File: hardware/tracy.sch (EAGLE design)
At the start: 68 parts, among them IC1 SIM900, J1 U.FL, J2 U.FL, Q4 si2305cd, T2 BC846, U1 SPX5205 3v3, U2 3339, U3 TC1014 2V8, Y1 32768Hz CFPX-217 12.5pF

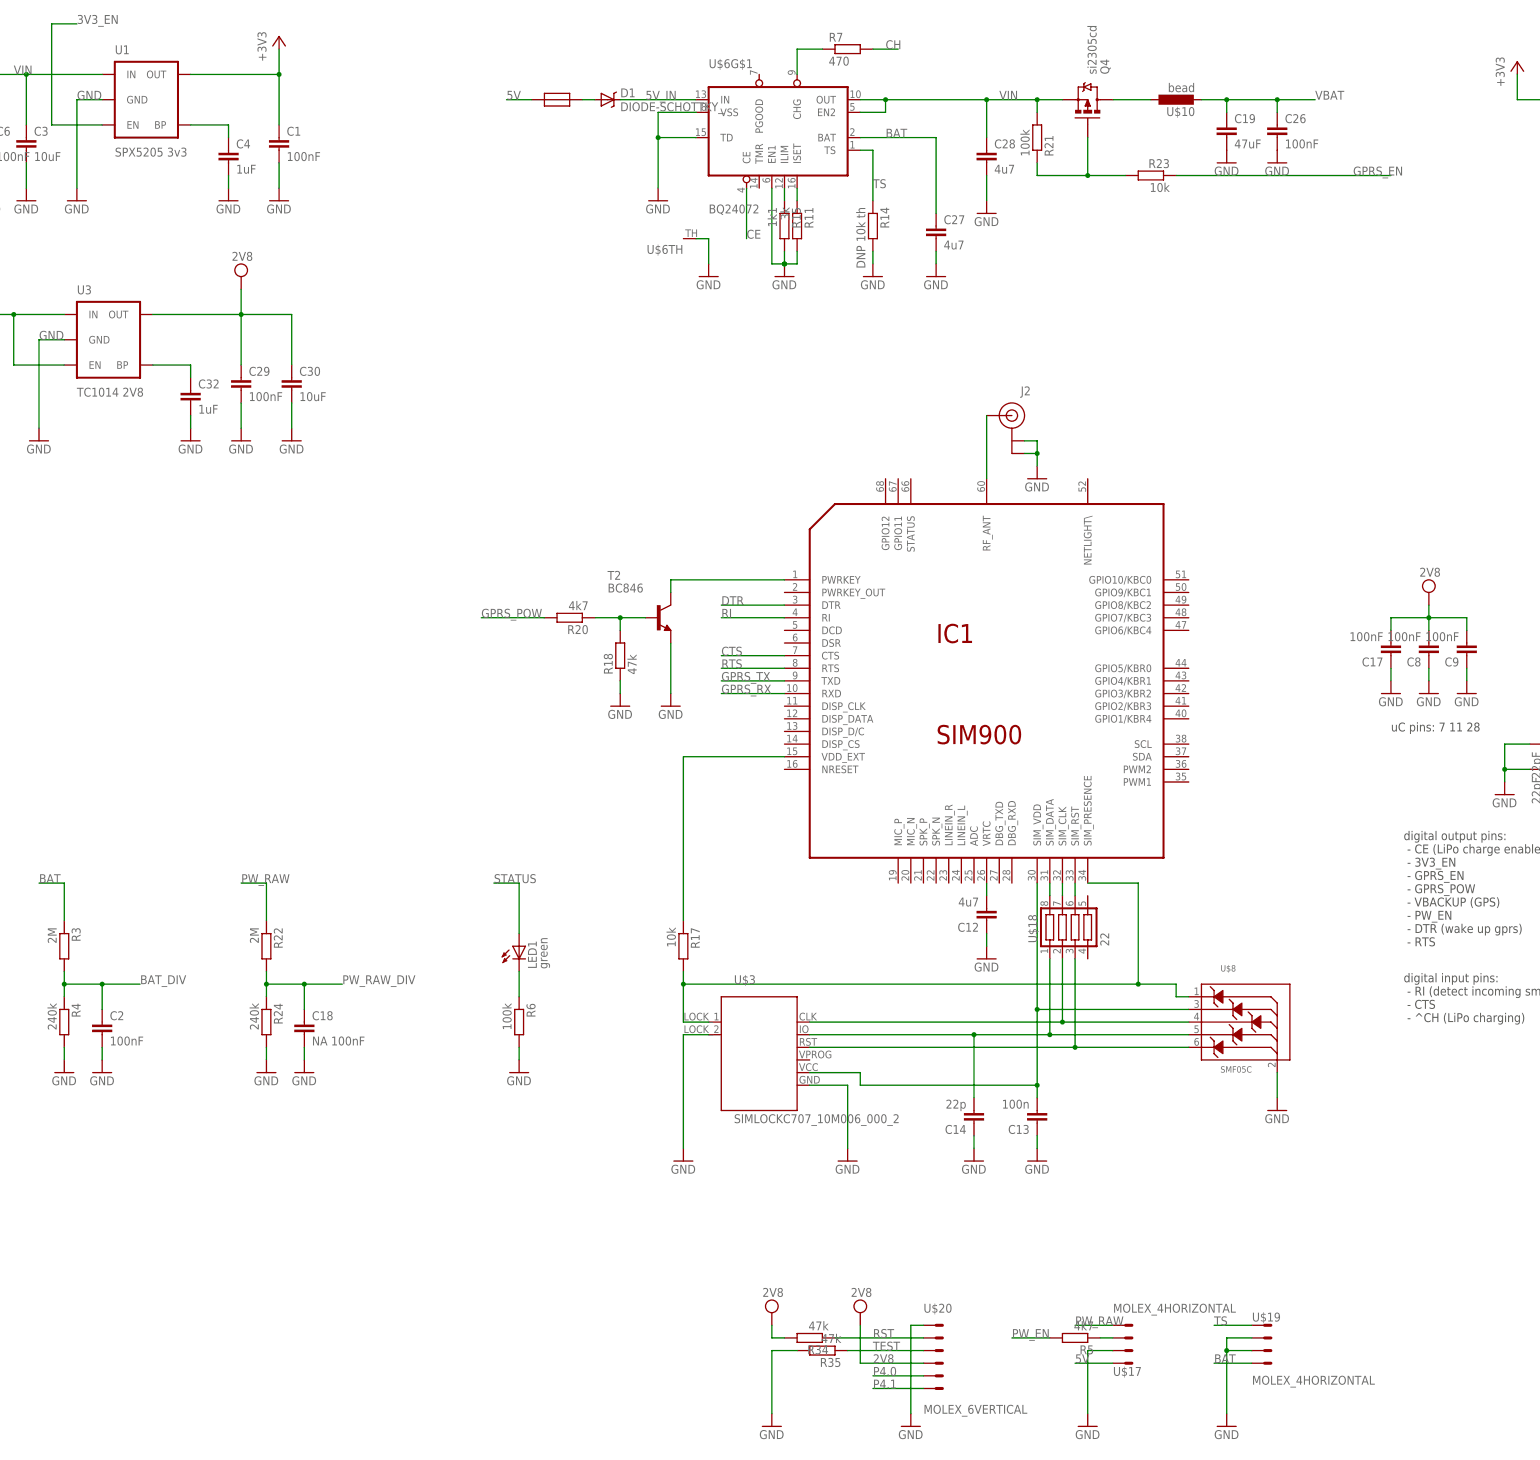
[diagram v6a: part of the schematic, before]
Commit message: add silkscreen
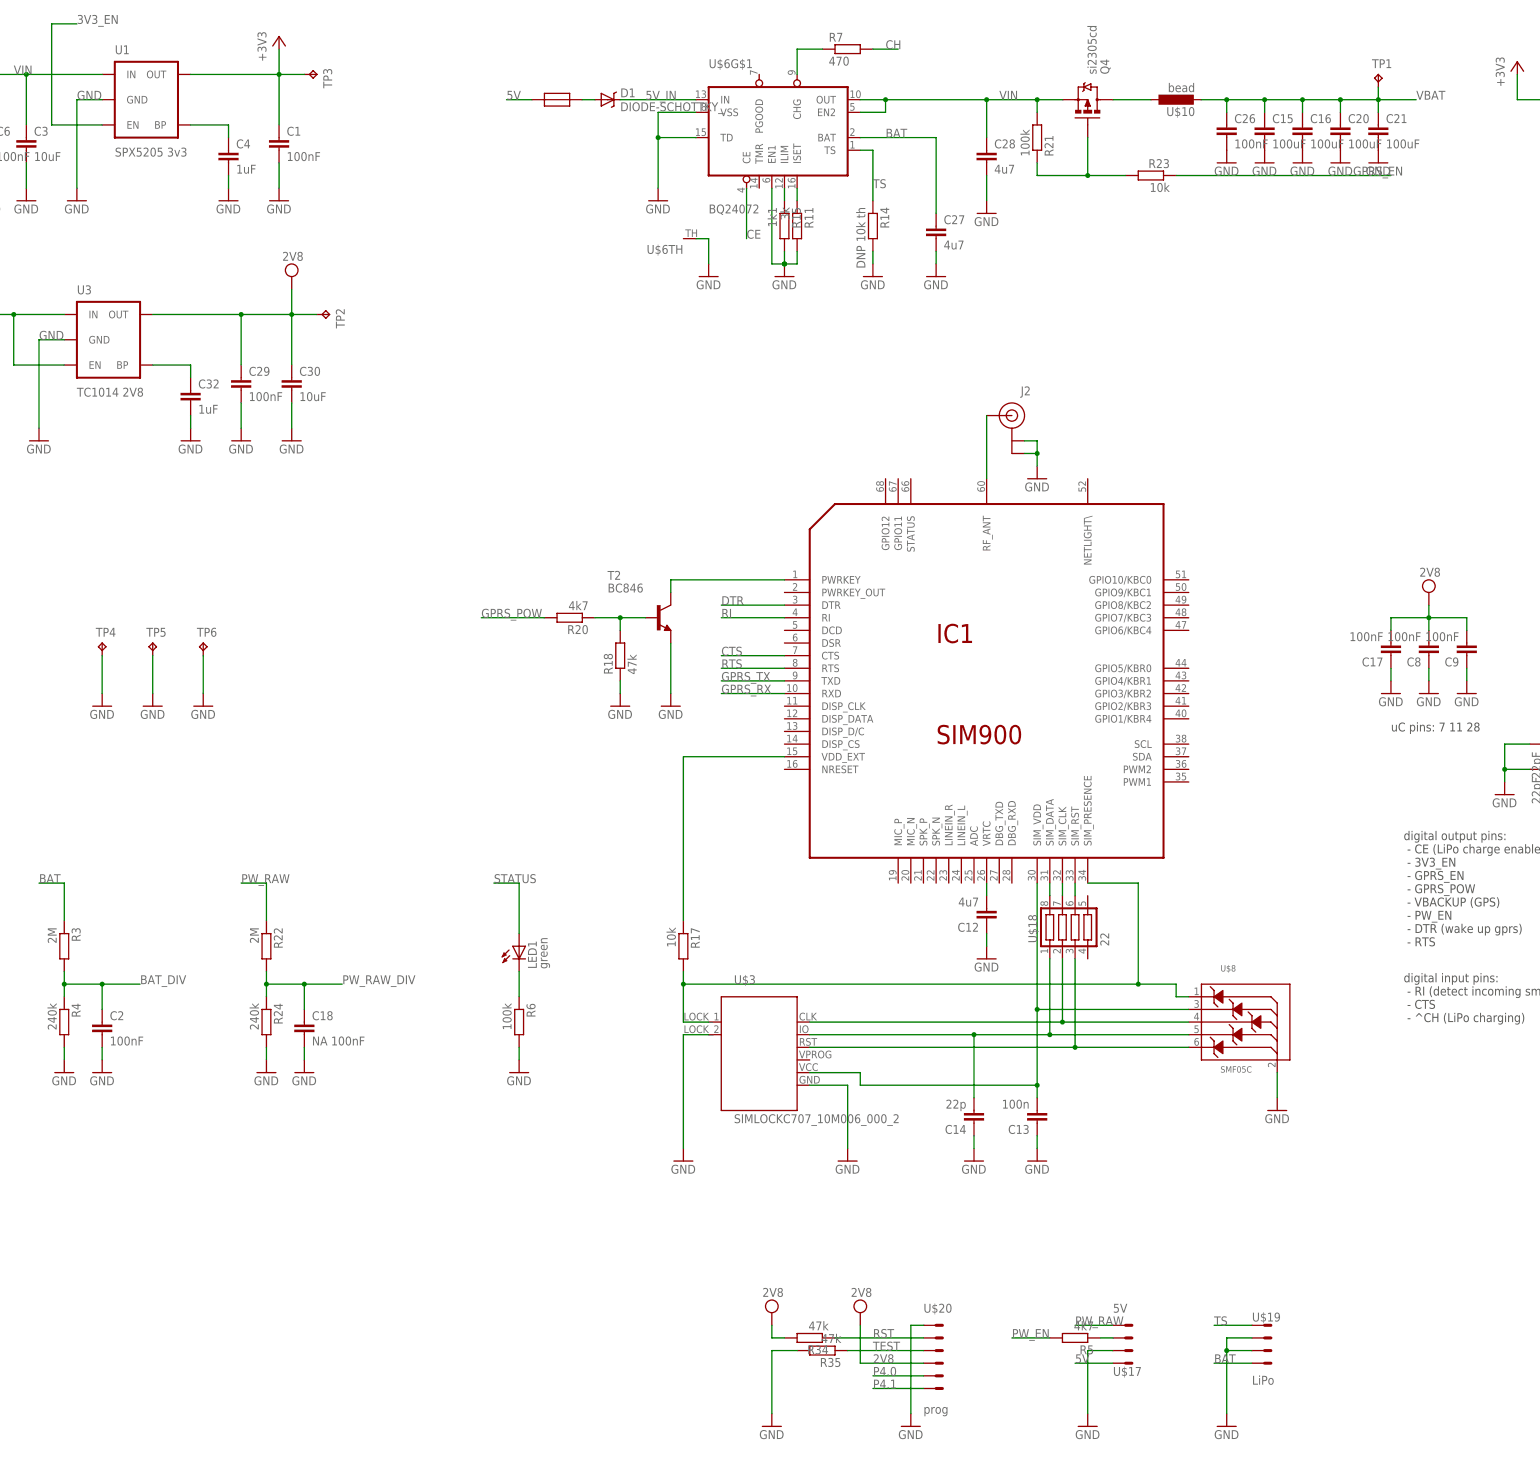
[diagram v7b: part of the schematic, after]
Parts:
- removed C19: 47uF, rcl:C-EUC1206
- added C15, C16, C20, C21: 100uF, rcl:C-EUC1206
- added TP1, TP2, TP3, TP4, TP5, TP6: TPTP12R, testpad:TPTP12R
- U$17: value MOLEX_4HORIZONTAL -> 5V
- U$19: value MOLEX_4HORIZONTAL -> LiPo
- U$20: value MOLEX_6VERTICAL -> prog
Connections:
- net +3V3: now also TP3.TP
- net 2V8: now also TP2.TP
- net GND: now also C15.2, C16.2, C20.2, C21.2, TP4.TP, TP5.TP, TP6.TP; no longer C19.2
- net VBAT: now also C15.1, C16.1, C20.1, C21.1, TP1.TP; no longer C19.1
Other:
- moved on the sheet: C26
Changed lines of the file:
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@@
 <part name="R23" library="rcl" deviceset="R-EU_" device="R0805W" value="10k"/>
 <part name="U$10" library="Simplex-rlc" deviceset="INDUCTOR" device="" value="bead"/>
-<part name="C19" library="rcl" deviceset="C-EU" device="C1206" value="47uF"/>
-<part name="GND19" library="SparkFun" deviceset="GND" device=""/>
 <part name="C26" library="rcl" deviceset="C-EU" device="C0805" value="100nF"/>
 <part name="GND40" library="SparkFun" deviceset="GND" device=""/>
@@
 <part name="GND1" library="SparkFun" deviceset="GND" device=""/>
 <part name="IC1" library="Simplex-ICs" deviceset="SIM900" device=""/>
-<part name="U$17" library="Simplex-Connectors" deviceset="MOLEX_4" device="HORIZONTAL"/>
-<part name="U$19" library="Simplex-Connectors" deviceset="MOLEX_4" device="HORIZONTAL"/>
-<part name="U$20" library="Simplex-Connectors" deviceset="MOLEX_6" device="VERTICAL"/>
+<part name="U$17" library="Simplex-Connectors" deviceset="MOLEX_4" device="HORIZONTAL" value="5V"/>
+<part name="U$19" library="Simplex-Connectors" deviceset="MOLEX_4" device="HORIZONTAL" value="LiPo"/>
+<part name="U$20" library="Simplex-Connectors" deviceset="MOLEX_6" device="VERTICAL" value="prog"/>
 <part name="R6" library="rcl" deviceset="R-EU_" device="R0805W" value="100k"/>
 <part name="GND36" library="SparkFun" deviceset="GND" device=""/>
 <part name="LED1" library="led" deviceset="LED" device="CHIPLED_0805" value="green"/>
 <part name="R7" library="rcl" deviceset="R-EU_" device="R0805W" value="470"/>
+<part name="C15" library="rcl" deviceset="C-EU" device="C1206" value="100uF"/>
+<part name="C16" library="rcl" deviceset="C-EU" device="C1206" value="100uF"/>
+<part name="C20" library="rcl" deviceset="C-EU" device="C1206" value="100uF"/>
+<part name="GND43" library="SparkFun" deviceset="GND" device=""/>
+<part name="GND44" library="SparkFun" deviceset="GND" device=""/>
+<part name="GND53" library="SparkFun" deviceset="GND" device=""/>
+<part name="C21" library="rcl" deviceset="C-EU" device="C1206" value="100uF"/>
+<part name="GND19" library="SparkFun" deviceset="GND" device=""/>
+<part name="TP1" library="testpad" deviceset="TP" device="TP12R"/>
+<part name="TP3" library="testpad" deviceset="TP" device="TP12R"/>
+<part name="TP2" library="testpad" deviceset="TP" device="TP12R"/>
+<part name="TP4" library="testpad" deviceset="TP" device="TP12R"/>
+<part name="GND55" library="SparkFun" deviceset="GND" device=""/>
+<part name="TP5" library="testpad" deviceset="TP" device="TP12R"/>
+<part name="GND56" library="SparkFun" deviceset="GND" device=""/>
+<part name="TP6" library="testpad" deviceset="TP" device="TP12R"/>
+<part name="GND57" library="SparkFun" deviceset="GND" device=""/>
 </parts>
 <sheets>
@@
 <instance part="R23" gate="G$1" x="238.76" y="264.16" rot="MR0"/>
 <instance part="U$10" gate="G$1" x="243.84" y="279.4" rot="R90"/>
-<instance part="C19" gate="G$1" x="254" y="274.32"/>
-<instance part="GND19" gate="1" x="254" y="266.7"/>
-<instance part="C26" gate="G$1" x="264.16" y="274.32"/>
-<instance part="GND40" gate="1" x="264.16" y="266.7"/>
+<instance part="C26" gate="G$1" x="254" y="274.32"/>
+<instance part="GND40" gate="1" x="254" y="266.7"/>
 <instance part="C27" gate="G$1" x="195.58" y="254"/>
 <instance part="GND41" gate="1" x="195.58" y="243.84"/>
@@
 <instance part="C32" gate="G$1" x="45.72" y="220.98"/>
 <instance part="GND54" gate="1" x="45.72" y="210.82"/>
-<instance part="U$4" gate="G$1" x="55.88" y="241.3"/>
+<instance part="U$4" gate="G$1" x="66.04" y="241.3"/>
 <instance part="U$11" gate="G$1" x="162.56" y="33.02"/>
 <instance part="U$12" gate="G$1" x="180.34" y="33.02"/>
@@
 <instance part="LED1" gate="G$1" x="111.76" y="109.22"/>
 <instance part="R7" gate="G$1" x="177.8" y="289.56"/>
+<instance part="C15" gate="G$1" x="261.62" y="274.32"/>
+<instance part="C16" gate="G$1" x="269.24" y="274.32"/>
+<instance part="C20" gate="G$1" x="276.86" y="274.32"/>
+<instance part="GND43" gate="1" x="261.62" y="266.7"/>
+<instance part="GND44" gate="1" x="269.24" y="266.7"/>
+<instance part="GND53" gate="1" x="276.86" y="266.7"/>
+<instance part="C21" gate="G$1" x="284.48" y="274.32"/>
+<instance part="GND19" gate="1" x="284.48" y="266.7"/>
+<instance part="TP1" gate="G$1" x="284.48" y="284.48"/>
+<instance part="TP3" gate="G$1" x="71.12" y="284.48" rot="R270"/>
+<instance part="TP2" gate="G$1" x="73.66" y="236.22" rot="R270"/>
+<instance part="TP4" gate="G$1" x="27.94" y="170.18"/>
+<instance part="GND55" gate="1" x="27.94" y="157.48"/>
+<instance part="TP5" gate="G$1" x="38.1" y="170.18"/>
+<instance part="GND56" gate="1" x="38.1" y="157.48"/>
+<instance part="TP6" gate="G$1" x="48.26" y="170.18"/>
+<instance part="GND57" gate="1" x="48.26" y="157.48"/>
 </instances>
 <busses>
@@
 </segment>
 <segment>
-<pinref part="C19" gate="G$1" pin="2"/>
-<pinref part="GND19" gate="1" pin="GND"/>
-</segment>
-<segment>
 <pinref part="C26" gate="G$1" pin="2"/>
 <pinref part="GND40" gate="1" pin="GND"/>
@@
 <pinref part="GND36" gate="1" pin="GND"/>
 <wire x1="111.76" y1="88.9" x2="111.76" y2="86.36" width="0.1524" layer="91"/>
+</segment>
+<segment>
+<pinref part="C15" gate="G$1" pin="2"/>
+<pinref part="GND43" gate="1" pin="GND"/>
+</segment>
+<segment>
+<pinref part="C16" gate="G$1" pin="2"/>
+<pinref part="GND44" gate="1" pin="GND"/>
+</segment>
+<segment>
+<pinref part="C20" gate="G$1" pin="2"/>
+<pinref part="GND53" gate="1" pin="GND"/>
+</segment>
+<segment>
+<pinref part="C21" gate="G$1" pin="2"/>
+<pinref part="GND19" gate="1" pin="GND"/>
+</segment>
+<segment>
+<pinref part="TP4" gate="G$1" pin="TP"/>
+<pinref part="GND55" gate="1" pin="GND"/>
+<wire x1="27.94" y1="167.64" x2="27.94" y2="160.02" width="0.1524" layer="91"/>
+</segment>
+<segment>
+<pinref part="TP5" gate="G$1" pin="TP"/>
+<pinref part="GND56" gate="1" pin="GND"/>
+<wire x1="38.1" y1="167.64" x2="38.1" y2="160.02" width="0.1524" layer="91"/>
+</segment>
+<segment>
+<pinref part="TP6" gate="G$1" pin="TP"/>
+<pinref part="GND57" gate="1" pin="GND"/>
+<wire x1="48.26" y1="167.64" x2="48.26" y2="160.02" width="0.1524" layer="91"/>
 </segment>
 </net>
@@
 <pinref part="C1" gate="G$1" pin="1"/>
 <pinref part="+3V1" gate="G$1" pin="+3V3"/>
+<pinref part="TP3" gate="G$1" pin="TP"/>
+<wire x1="63.5" y1="284.48" x2="68.58" y2="284.48" width="0.1524" layer="91"/>
 </segment>
 <segment>
@@
 <pinref part="U$10" gate="G$1" pin="2"/>
 <wire x1="248.92" y1="279.4" x2="254" y2="279.4" width="0.1524" layer="91"/>
-<pinref part="C19" gate="G$1" pin="1"/>
+<pinref part="C26" gate="G$1" pin="1"/>
 <wire x1="254" y1="279.4" x2="254" y2="276.86" width="0.1524" layer="91"/>
+<wire x1="254" y1="279.4" x2="261.62" y2="279.4" width="0.1524" layer="91"/>
 <junction x="254" y="279.4"/>
-<wire x1="254" y1="279.4" x2="264.16" y2="279.4" width="0.1524" layer="91"/>
-<pinref part="C26" gate="G$1" pin="1"/>
-<wire x1="264.16" y1="279.4" x2="264.16" y2="276.86" width="0.1524" layer="91"/>
-<wire x1="264.16" y1="279.4" x2="271.78" y2="279.4" width="0.1524" layer="91"/>
-<junction x="264.16" y="279.4"/>
-<label x="271.78" y="279.4" size="1.778" layer="95"/>
+<label x="292.1" y="279.4" size="1.778" layer="95"/>
+<pinref part="C15" gate="G$1" pin="1"/>
+<wire x1="261.62" y1="279.4" x2="269.24" y2="279.4" width="0.1524" layer="91"/>
+<wire x1="269.24" y1="279.4" x2="276.86" y2="279.4" width="0.1524" layer="91"/>
+<wire x1="276.86" y1="279.4" x2="284.48" y2="279.4" width="0.1524" layer="91"/>
+<wire x1="284.48" y1="279.4" x2="292.1" y2="279.4" width="0.1524" layer="91"/>
+<wire x1="261.62" y1="276.86" x2="261.62" y2="279.4" width="0.1524" layer="91"/>
+<pinref part="C16" gate="G$1" pin="1"/>
+<wire x1="269.24" y1="276.86" x2="269.24" y2="279.4" width="0.1524" layer="91"/>
+<pinref part="C20" gate="G$1" pin="1"/>
+<wire x1="276.86" y1="276.86" x2="276.86" y2="279.4" width="0.1524" layer="91"/>
+<junction x="261.62" y="279.4"/>
+<junction x="269.24" y="279.4"/>
+<junction x="276.86" y="279.4"/>
+<pinref part="C21" gate="G$1" pin="1"/>
+<wire x1="284.48" y1="276.86" x2="284.48" y2="279.4" width="0.1524" layer="91"/>
+<junction x="284.48" y="279.4"/>
+<pinref part="TP1" gate="G$1" pin="TP"/>
+<wire x1="284.48" y1="281.94" x2="284.48" y2="279.4" width="0.1524" layer="91"/>
 </segment>
 </net>
@@
 <net name="2V8" class="0">
 <segment>
-<pinref part="U$4" gate="G$1" pin="2V8"/>
-<pinref part="C29" gate="G$1" pin="1"/>
-<wire x1="55.88" y1="241.3" x2="55.88" y2="236.22" width="0.1524" layer="91"/>
-<pinref part="U3" gate="G$1" pin="OUT"/>
-<wire x1="55.88" y1="236.22" x2="55.88" y2="226.06" width="0.1524" layer="91"/>
-<wire x1="38.1" y1="236.22" x2="55.88" y2="236.22" width="0.1524" layer="91"/>
-<pinref part="C30" gate="G$1" pin="1"/>
-<wire x1="55.88" y1="236.22" x2="66.04" y2="236.22" width="0.1524" layer="91"/>
-<wire x1="66.04" y1="236.22" x2="66.04" y2="226.06" width="0.1524" layer="91"/>
-<junction x="55.88" y="236.22"/>
-</segment>
-<segment>
 <wire x1="162.56" y1="33.02" x2="162.56" y2="30.48" width="0.1524" layer="91"/>
 <pinref part="R34" gate="G$1" pin="2"/>
@@
 <pinref part="U$16" gate="G$1" pin="2V8"/>
 </segment>
-</net>
+<segment>
+<pinref part="C29" gate="G$1" pin="1"/>
+<pinref part="U3" gate="G$1" pin="OUT"/>
+<wire x1="55.88" y1="236.22" x2="55.88" y2="226.06" width="0.1524" layer="91"/>
+<wire x1="38.1" y1="236.22" x2="55.88" y2="236.22" width="0.1524" layer="91"/>
+<pinref part="C30" gate="G$1" pin="1"/>
+<wire x1="55.88" y1="236.22" x2="66.04" y2="236.22" width="0.1524" layer="91"/>
+<wire x1="66.04" y1="236.22" x2="66.04" y2="226.06" width="0.1524" layer="91"/>
+<junction x="55.88" y="236.22"/>
+<pinref part="U$4" gate="G$1" pin="2V8"/>
+<wire x1="66.04" y1="241.3" x2="66.04" y2="236.22" width="0.1524" layer="91"/>
+<junction x="66.04" y="236.22"/>
+<pinref part="TP2" gate="G$1" pin="TP"/>
+<wire x1="66.04" y1="236.22" x2="71.12" y2="236.22" width="0.1524" layer="91"/>
+</segment>
+</net>

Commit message: checks
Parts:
- removed R2: 2k2, rcl:R-EU_R0805W
- removed R7: 470, rcl:R-EU_R0805W
- removed TP1: TPTP12R, testpad:TPTP12R
- added R8: 330, rcl:R-EU_R0805W
- added T1: BC846, transistor:BC846
- C11: value 220nF -> 10uF
- C18: value NA 100nF -> DNP 100nF
- R21: value 100k -> 10k
- R24: value 240k -> 240K
- R4: value 240k -> 1M3
- R5: value 4k7 -> 1k
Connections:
- removed net N$5: R2.2, U$1.34, U$2.1
- removed net VBACKUP: R1.2, U$1.35, U2.VBACKUP
- new net GPS_BKP: R8.2, U$1.35
- new net N$11: C11.1, R1.2, R8.1, U2.VBACKUP
- net CH: now also U$6G$1.CHG; no longer R7.2
- net GND: now also T1.E, U$1.39, U$1.41; no longer R2.1
- net GPRS_EN: now also U$1.22; no longer U$1.21
- net GPRS_POW: now also U$1.21; no longer U$1.22
- net N$10: now also U$1.34, U$2.1; no longer R7.1, U$6G$1.CHG
- net N$48: now also T1.C; no longer R23.2
- net N$7: now also R23.2, T1.B; no longer C11.1, U$1.43
- net VBAT: no longer TP1.TP
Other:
- moved on the sheet: C11, C15, C16, C20, C21, C26, J1, R1, R17, R21, R23, U$10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
